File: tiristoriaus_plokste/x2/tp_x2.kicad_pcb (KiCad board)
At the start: 2 copper layers, 62 x 84 mm, 74 parts, among them X1 LD3, X10 Faston_6.3x08x14, X11 Faston_6.3x08x14, X12 Faston_6.3x08x14, X13 Faston_6.3x08x14, X14 Faston_6.3x08x14, X17 Faston_6.3x08x14, X2 PH3, X26 Faston_6.3x08x14, X3 Faston_6.3x08x14, X4 LD1, X5 PH1, X6 Faston_6.3x08x14, X7 Faston_6.3x08x14, X8 Faston_6.3x08x14, X9 Faston_6.3x08x14

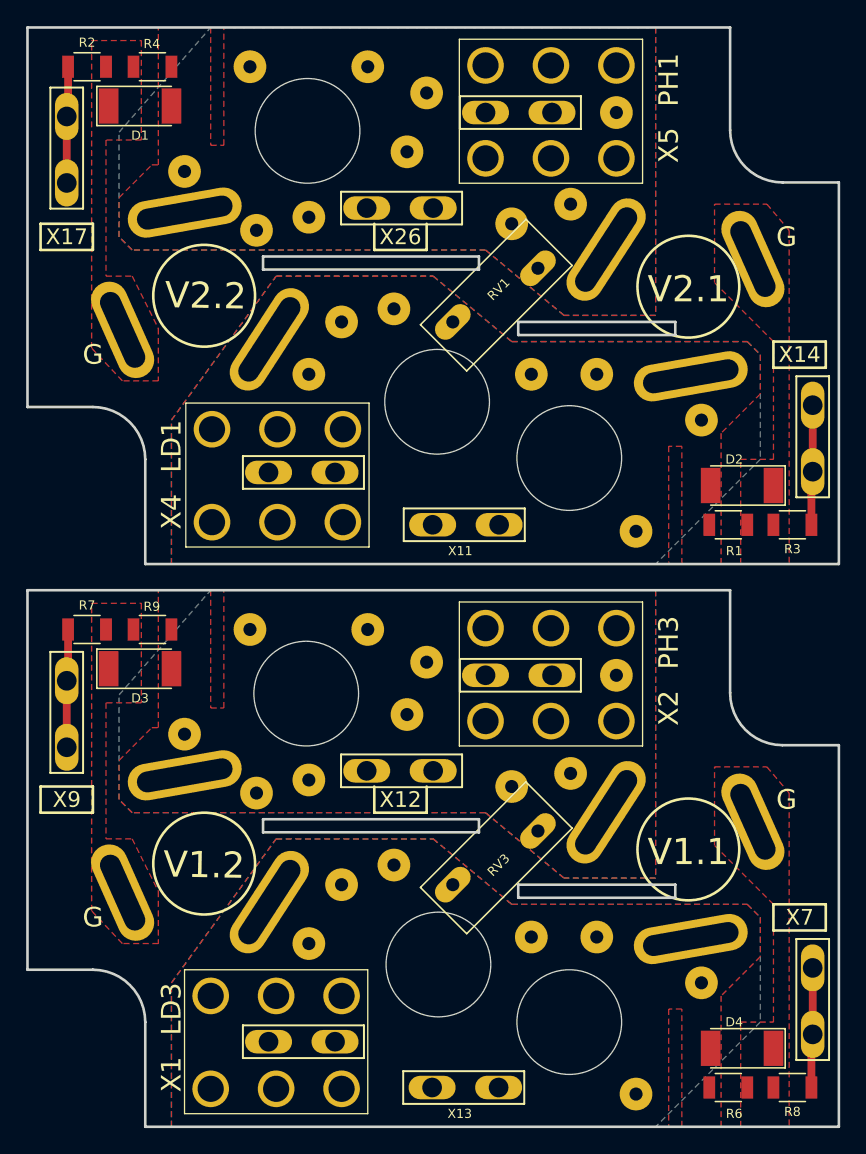
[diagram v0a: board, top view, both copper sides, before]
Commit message: sugeneruoti nauji gerberiai, paruostos principine ir surinkimo schemos.
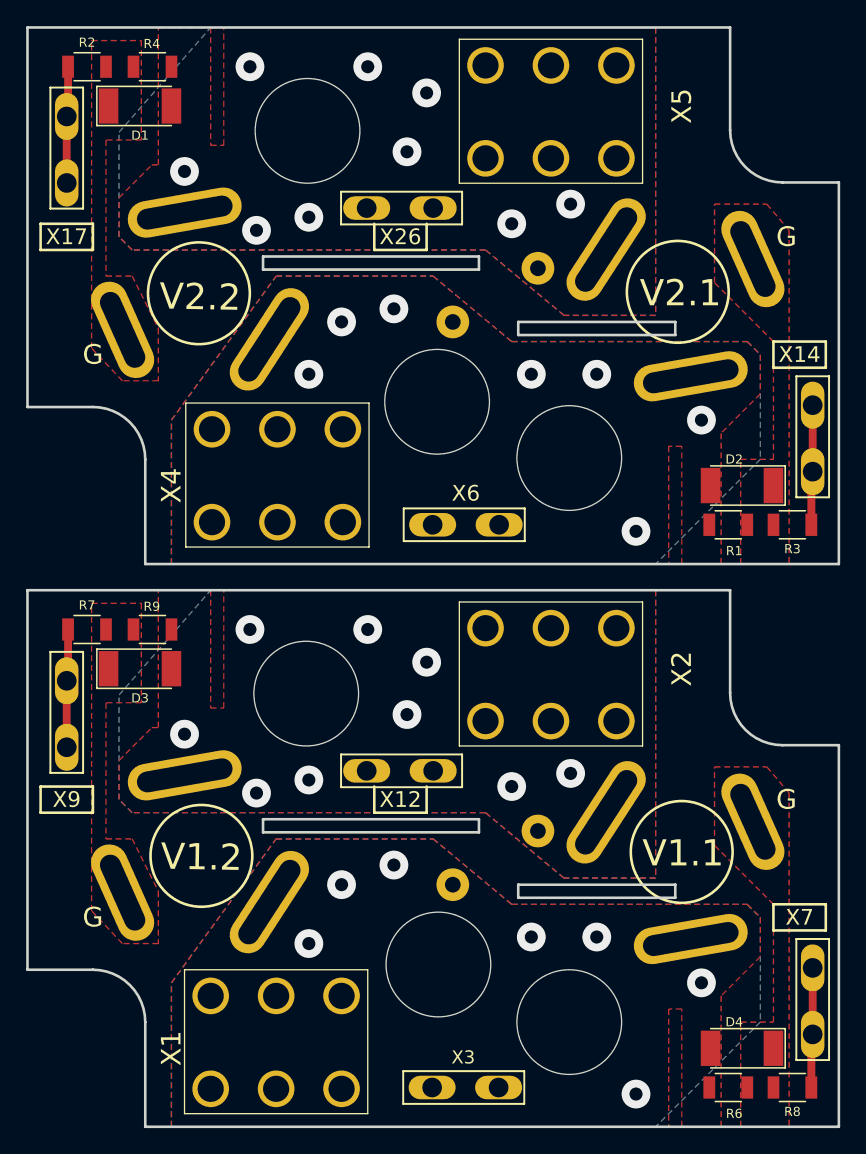
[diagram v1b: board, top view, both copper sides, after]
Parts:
- removed H10, H11, H12, H13, H14, H15, H16, H17, H18, H19, H20, H22, H23, H24, H27, H28, H29, H30, H31, H32, H33, H34, H35, H36, H37, H38, H39, H40, H5, H6, H9: Conn_01x01, Wire_Pads:SolderWirePad_single_1mmDrill
- removed RV1, RV3: 480V, disc:VR_VE420V
- removed X10, X8: Faston_6.3x08x14, mech:Faston_6.3x0.8x14
- removed the X3 at (100.0, 80.0)
- removed the X6 at (116.5, 52.5)
- added H4: Conn_01x01, Wire_Pads:SolderWirePad_single_1mmDrill, F.Cu at (118.0, 64.4)
- X1: value LD3 -> LD1
- X2: value PH3 -> PH1
- X4: value LD1 -> LD3
- X5: value PH1 -> PH3
- moved H1 43.8 mm to (111.5, 111.5)
- moved H2 41.4 mm to (118.0, 107.4)
- moved H3 21.3 mm to (111.5, 68.5)
- renumbered X13 to X3, X11 to X6
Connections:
- D1 pad 2: /PH1 -> /PH3
- D2 pad 2: /LD1 -> /LD3
- D3 pad 2: /PH3 -> /PH1
- D4 pad 2: /LD3 -> /LD1
- H2 pad 1: /LD1 -> /PH1
- H3 pad 1: /LD1 -> /LD3
- R1 pad 1: /LD1 -> /LD3
- R2 pad 1: /CTRL1A -> /CTRL3A
- R3 pad 1: /CTRL1B -> /CTRL3B
- R4 pad 1: /PH1 -> /PH3
- R6 pad 1: /LD3 -> /LD1
- R7 pad 1: /CTRL3A -> /CTRL1A
- R8 pad 1: /CTRL3B -> /CTRL1B
- R9 pad 1: /PH3 -> /PH1
- V1.1 pad 1: /PH3 -> /PH1
- V1.1 pad 3: /LD3 -> /LD1
- V1.2 pad 1: /LD3 -> /LD1
- V1.2 pad 3: /PH3 -> /PH1
- V2.1 pad 1: /PH1 -> /PH3
- V2.1 pad 3: /LD1 -> /LD3
- V2.2 pad 1: /LD1 -> /LD3
- V2.2 pad 3: /PH1 -> /PH3
- X1 pad 1: /LD3 -> /LD1
- X12 pad 1: /PH3 -> /PH1
- X14 pad 1: /CTRL1B -> /CTRL3B
- X17 pad 1: /CTRL1A -> /CTRL3A
- X2 pad 1: /PH3 -> /PH1
- X26 pad 1: /PH1 -> /PH3
- X3 pad 1: /LD3 -> /LD1
- X4 pad 1: /LD1 -> /LD3
- X5 pad 1: /PH1 -> /PH3
- X6 pad 1: /LD1 -> /LD3
- X7 pad 1: /CTRL3B -> /CTRL1B
- X9 pad 1: /CTRL3A -> /CTRL1A
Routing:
- net /PH3: vias 0 -> 9
- net /PH1: vias 0 -> 9
- net /LD3: vias 0 -> 7
- net /LD1: vias 0 -> 7
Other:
- board text added: "V1.1"
- board text added: "V1.2"
- board text added: "V2.1"
- board text added: "V2.2"
- board text added: "X1"
- board text added: "X11"
- board text added: "X12"
- board text added: "X13"
- board text added: "X14"
- board text added: "X17"
- board text added: "X2"
- board text added: "X26"
- board text added: "X4"
- board text added: "X5"
- board text added: "X7"
- board text added: "X9"

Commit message: paskutinis variantas. sugeneruoti nauji gerberiai
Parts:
- renumbered V1.2 to V1.1, V1.1 to V1.2, V2.2 to V2.1, V2.1 to V2.2
